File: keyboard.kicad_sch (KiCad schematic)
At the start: 23 parts, among them Q1 BSS138, Q2 BSS138, Q3 BSS138, Q4 BSS138, Q5 BSS138, Q6 BSS138, U4 BBQ20KBD, U5 ME6212C18M5G, U6 ME6212C28M5G

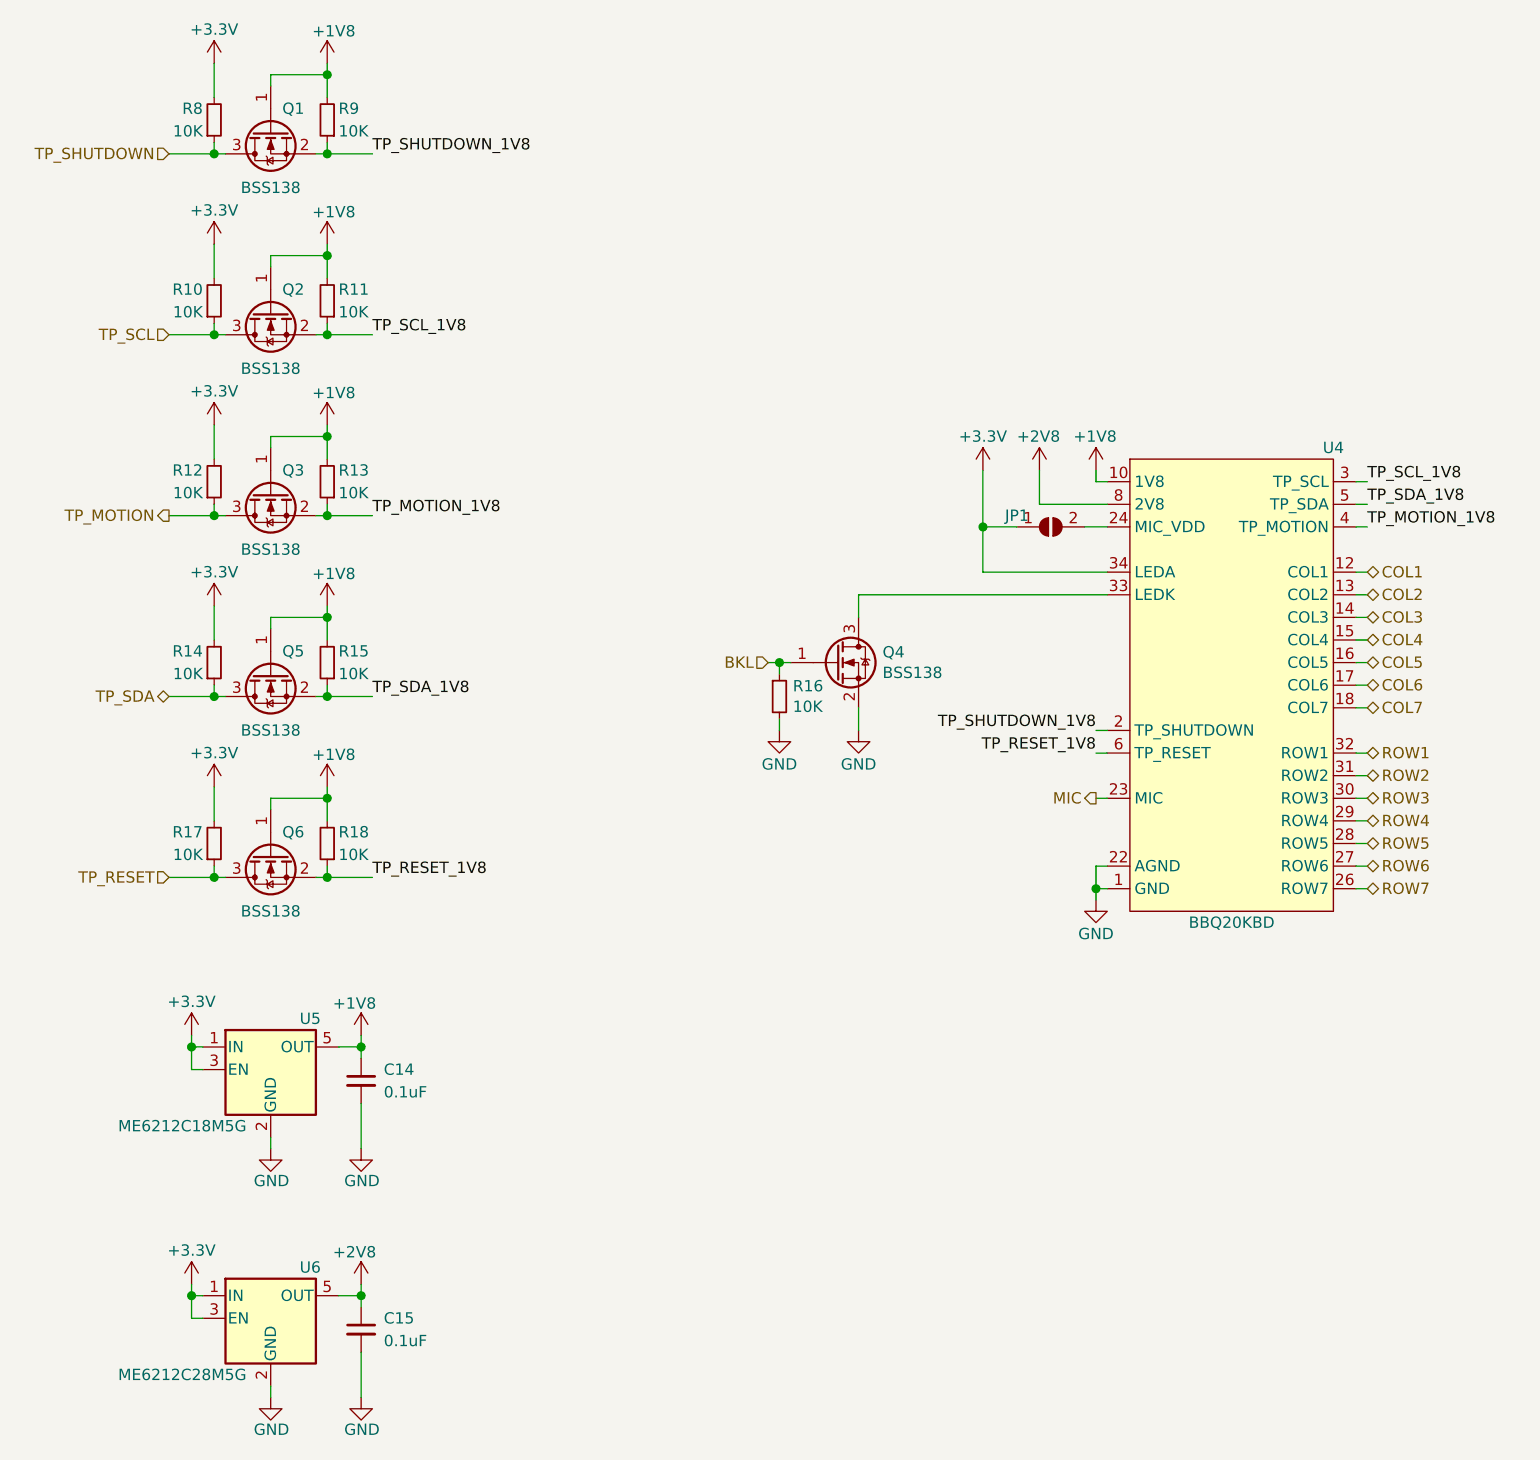
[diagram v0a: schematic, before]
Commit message: Migrate KiCAD version -> 1.0, update part numbers
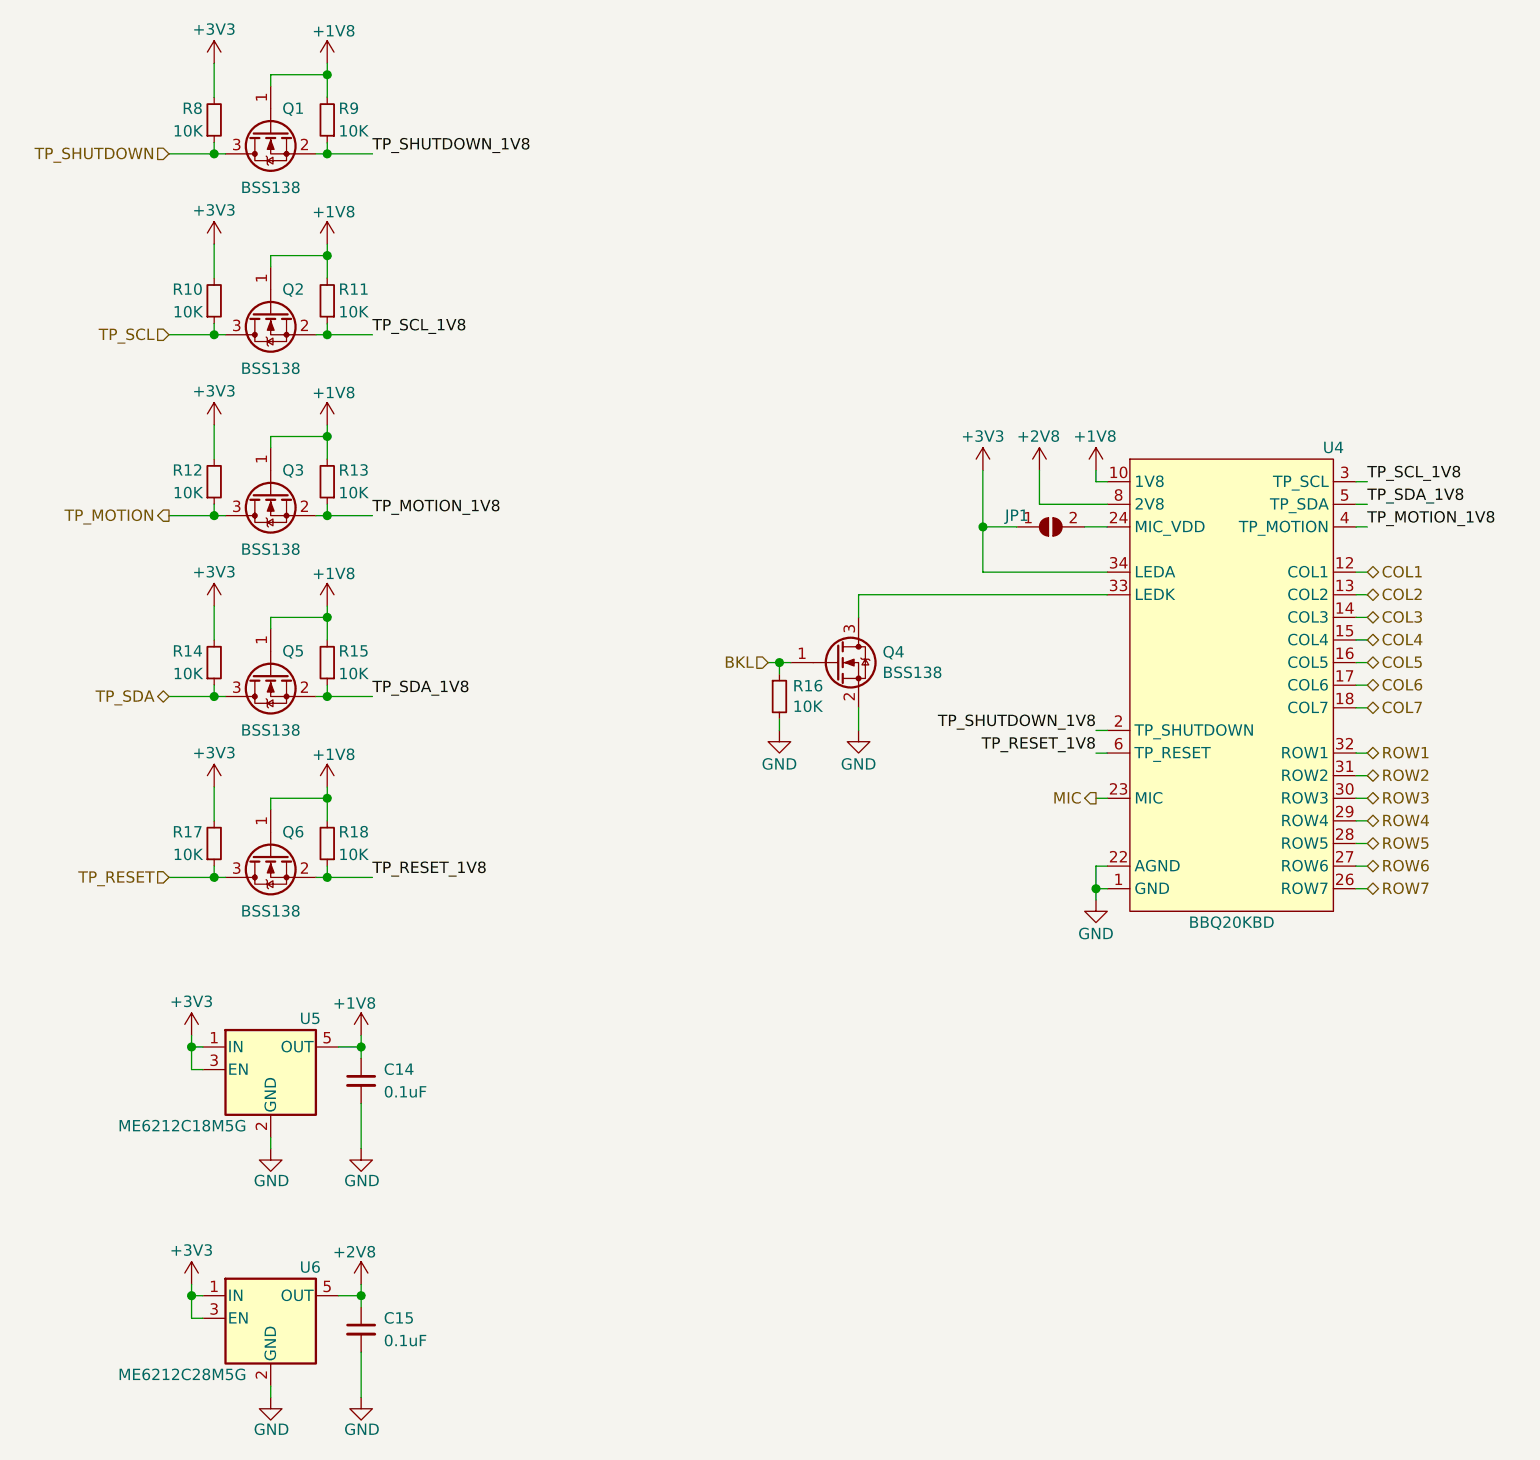
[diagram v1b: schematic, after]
